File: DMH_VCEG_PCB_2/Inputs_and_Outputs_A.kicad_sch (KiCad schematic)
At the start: 39 parts, among them J1 TS_Jack_6.35mm_Sw, J10 TS_Jack_6.35mm_Sw, J2 TS_Jack_6.35mm_Sw, J200 IDC_02x08, J21 Conn_01x10_PinHeader, J22 Conn_01x10_PinHeader, J23 Conn_01x10_PinHeader, J27 Conn_01x06_PinHeader, J3 TS_Jack_6.35mm_Sw, J4 TS_Jack_6.35mm_Sw, J5 TS_Jack_6.35mm_Sw, J6 TS_Jack_6.35mm_Sw, J7 TS_Jack_6.35mm_Sw, J8 TS_Jack_6.35mm_Sw, J9 TS_Jack_6.35mm_Sw, U21 TL074, U9 TL074

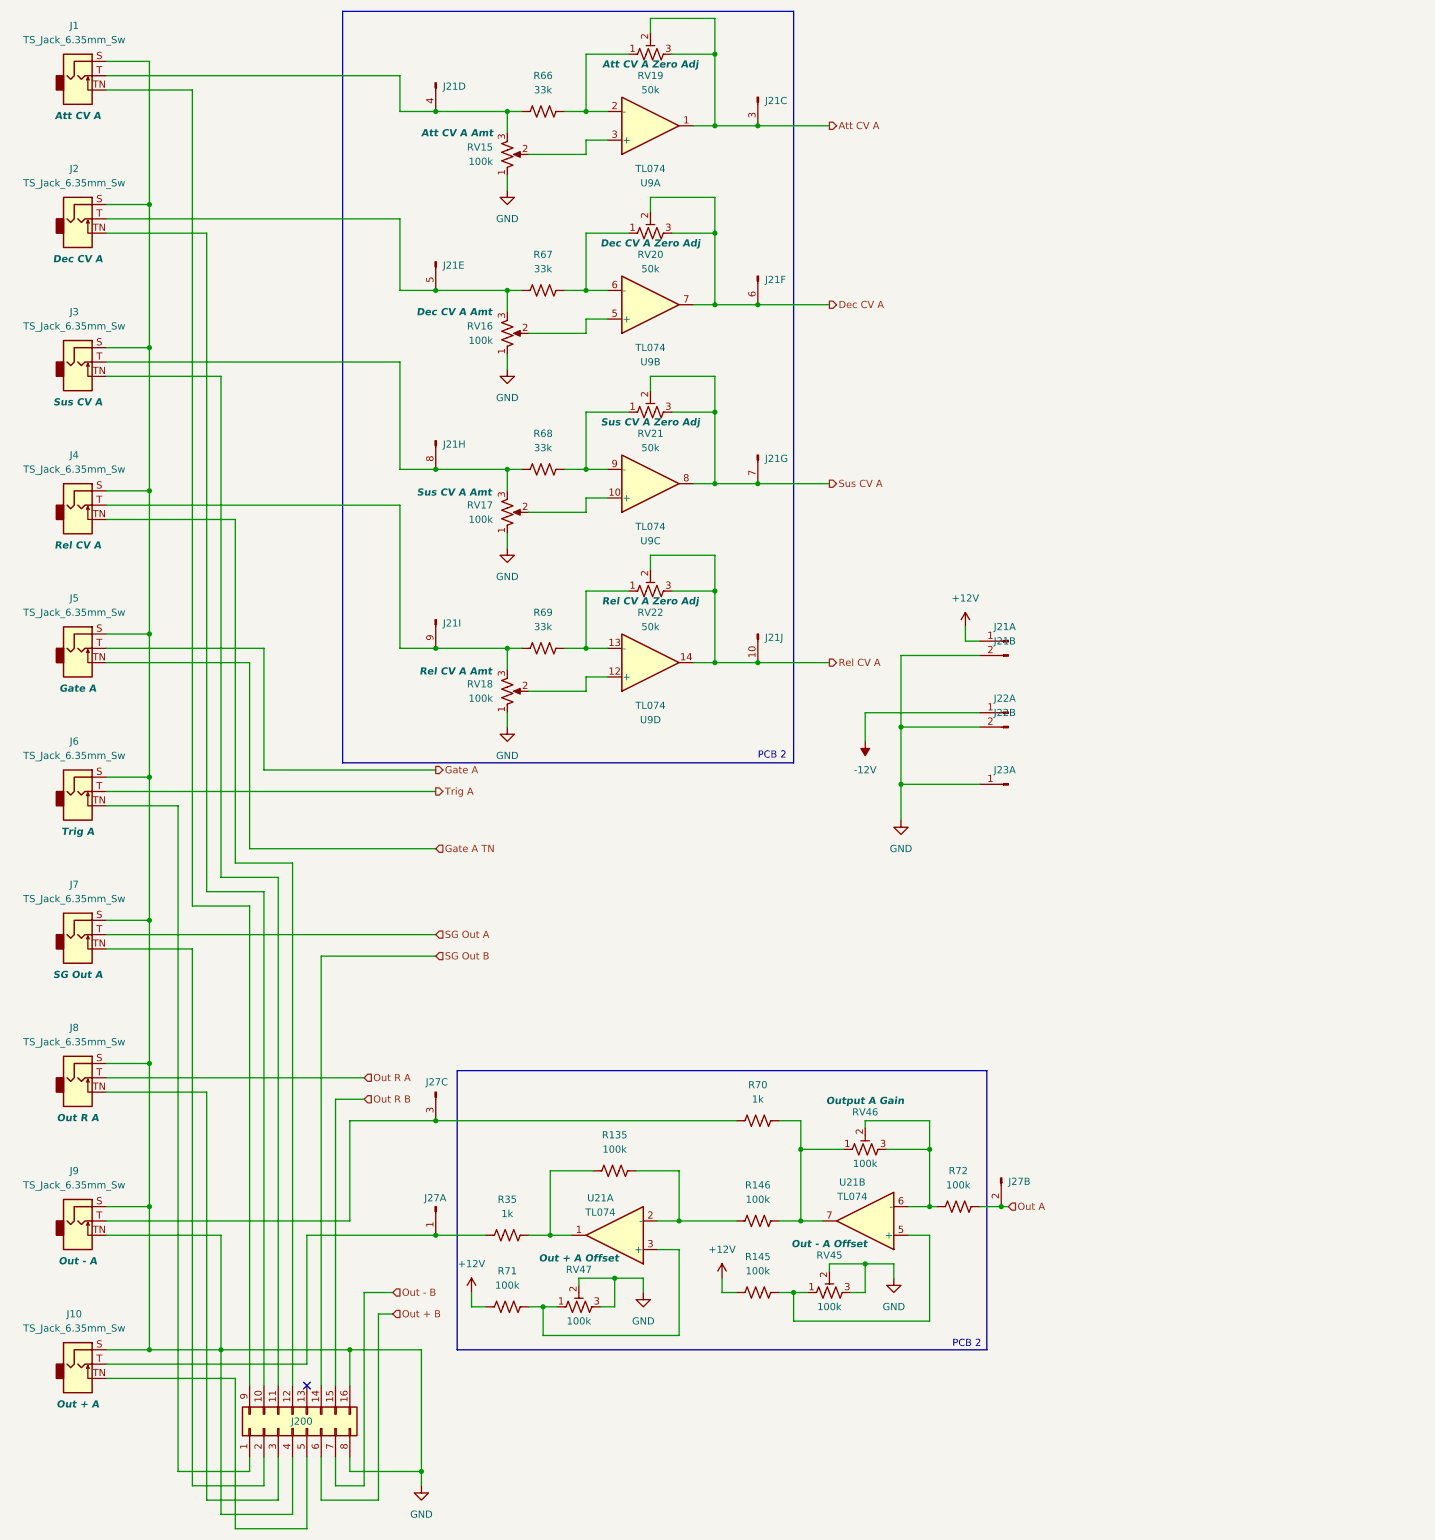
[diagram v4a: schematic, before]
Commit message: Fixed mistake in IO connections
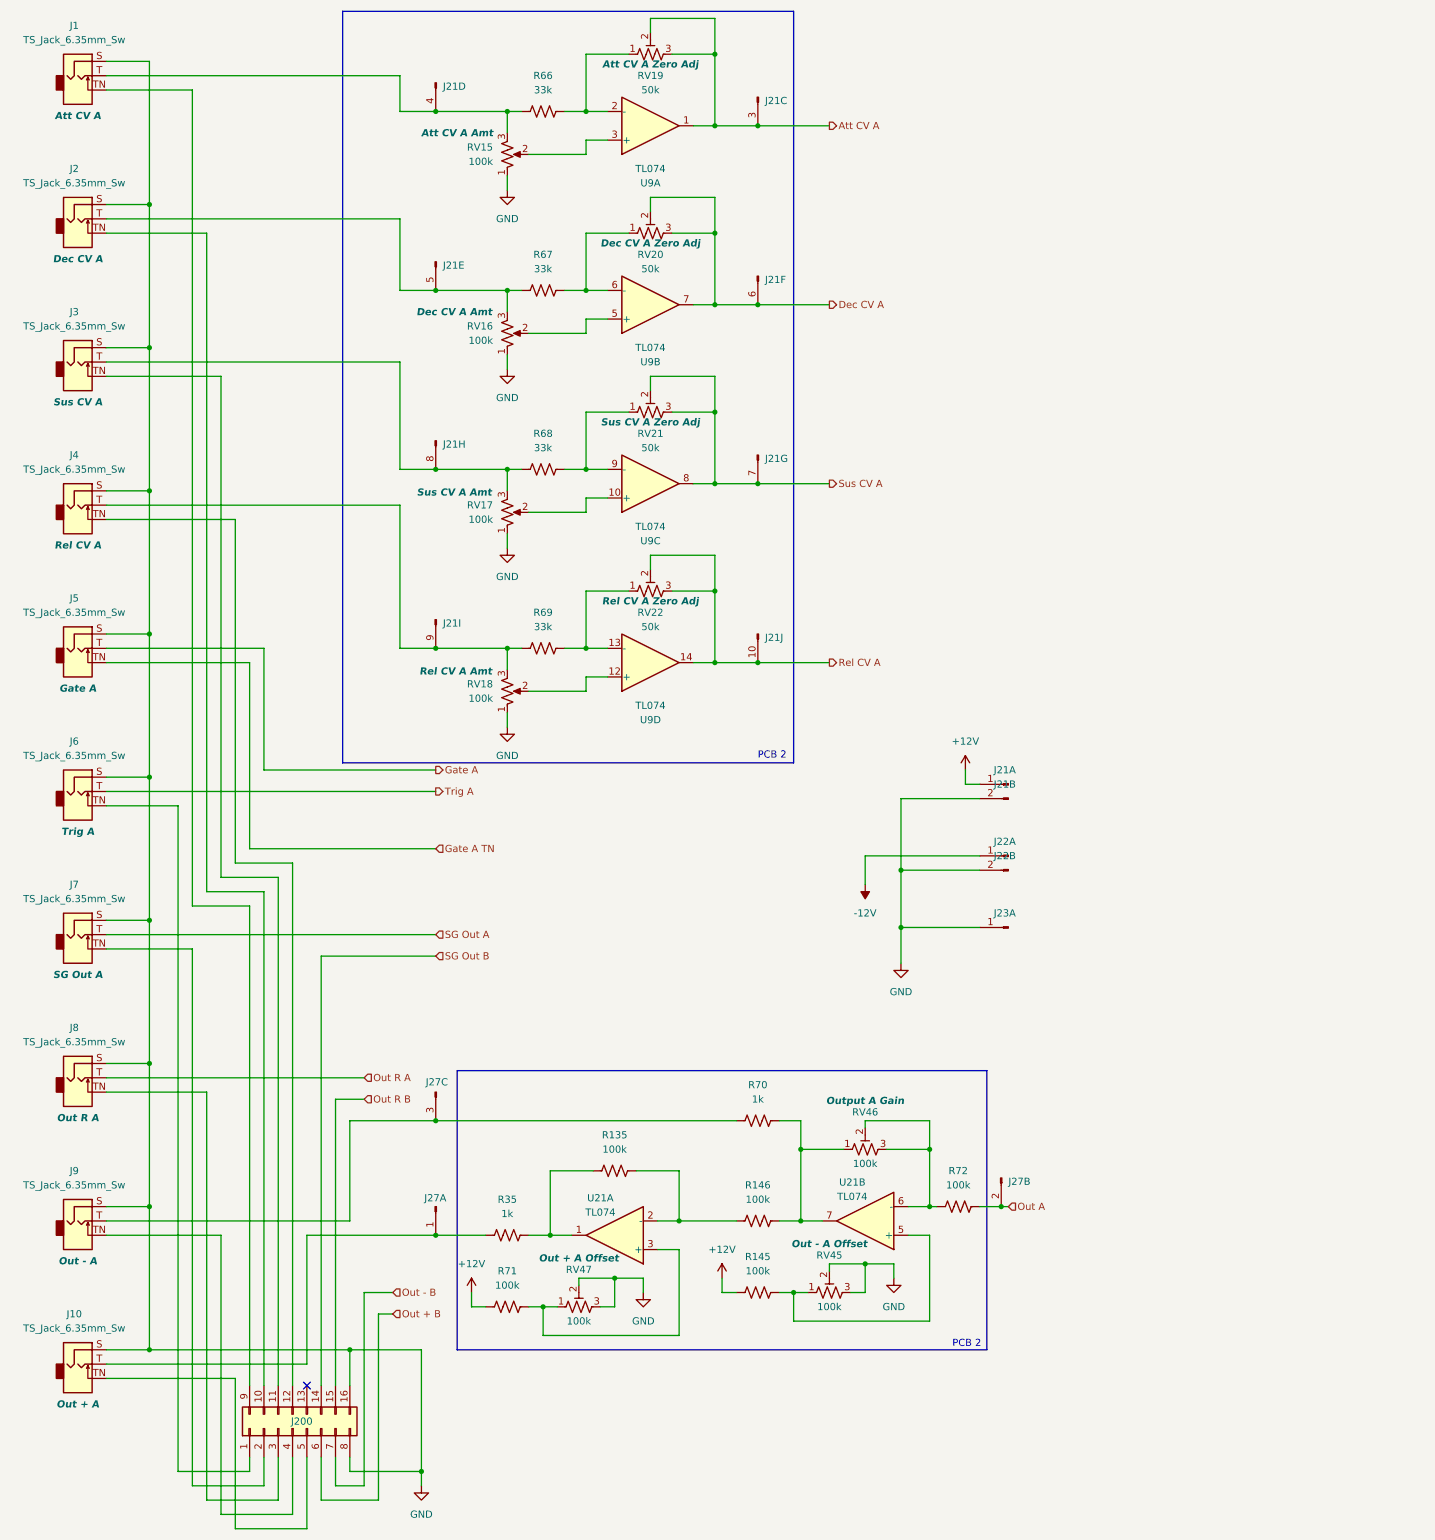
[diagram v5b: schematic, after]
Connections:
- net GND: no longer J200.4 (Pin_4), J9.TN
- new net: J200.4 (Pin_4), J9.TN
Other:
- moved on the sheet: J21A, J21B, J22A, J22B, J23A
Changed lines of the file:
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@@
 	)
 	(junction
-		(at 171.45 151.13)
+		(at 171.45 176.53)
 		(diameter 0)
 		(color 0 0 0 0)
@@
 	)
 	(junction
-		(at 171.45 140.97)
+		(at 171.45 166.37)
 		(diameter 0)
 		(color 0 0 0 0)
@@
 	)
 	(junction
-		(at 50.8 251.46)
-		(diameter 0)
-		(color 0 0 0 0)
-	)
-	(junction
 		(at 146.05 66.04)
 		(diameter 0)
@@
 	(wire
 		(pts
-			(xy 185.42 140.97) (xy 171.45 140.97)
+			(xy 185.42 166.37) (xy 171.45 166.37)
 		)
 		(stroke
@@
 	(wire
 		(pts
-			(xy 50.8 231.14) (xy 50.8 251.46)
+			(xy 50.8 231.14) (xy 50.8 280.67)
 		)
 		(stroke
@@
 	(wire
 		(pts
-			(xy 185.42 138.43) (xy 165.1 138.43)
+			(xy 185.42 163.83) (xy 165.1 163.83)
 		)
 		(stroke
@@
 	(wire
 		(pts
-			(xy 171.45 151.13) (xy 185.42 151.13)
+			(xy 171.45 176.53) (xy 185.42 176.53)
 		)
 		(stroke
@@
 	(wire
 		(pts
-			(xy 50.8 251.46) (xy 50.8 280.67)
-		)
-		(stroke
-			(width 0)
-			(type default)
-		)
-	)
-	(wire
-		(pts
 			(xy 139.7 241.3) (xy 142.24 241.3)
 		)
@@
 	(wire
 		(pts
-			(xy 185.42 128.27) (xy 171.45 128.27)
+			(xy 185.42 153.67) (xy 171.45 153.67)
 		)
 		(stroke
@@
 	(wire
 		(pts
-			(xy 171.45 140.97) (xy 171.45 151.13)
+			(xy 171.45 166.37) (xy 171.45 176.53)
 		)
 		(stroke
@@
 	(wire
 		(pts
-			(xy 171.45 128.27) (xy 171.45 140.97)
+			(xy 171.45 153.67) (xy 171.45 166.37)
 		)
 		(stroke
@@
 	(wire
 		(pts
-			(xy 50.8 251.46) (xy 38.1 251.46)
+			(xy 38.1 251.46) (xy 73.66 251.46)
 		)
 		(stroke
@@
 	(wire
 		(pts
-			(xy 182.88 123.19) (xy 182.88 125.73)
+			(xy 182.88 148.59) (xy 182.88 151.13)
 		)
 		(stroke
@@
 	(wire
 		(pts
-			(xy 165.1 138.43) (xy 165.1 143.51)
+			(xy 165.1 163.83) (xy 165.1 168.91)
 		)
 		(stroke
@@
 	(wire
 		(pts
-			(xy 185.42 125.73) (xy 182.88 125.73)
+			(xy 185.42 151.13) (xy 182.88 151.13)
 		)
 		(stroke
@@
 	(wire
 		(pts
-			(xy 171.45 151.13) (xy 171.45 157.48)
+			(xy 171.45 176.53) (xy 171.45 182.88)
 		)
 		(stroke
@@
 	(wire
 		(pts
-			(xy 50.8 251.46) (xy 73.66 251.46)
-		)
-		(stroke
-			(width 0)
-			(type default)
-		)
-	)
-	(wire
-		(pts
 			(xy 82.55 25.4) (xy 82.55 31.75)
 		)
@@
 	(symbol
 		(lib_id "SynthStuff:Conn_01x10_PinHeader")
-		(at 190.5 138.43 180)
+		(at 190.5 163.83 180)
 		(unit 1)
 		(exclude_from_sim no)
@@
 		(fields_autoplaced yes)
 		(property "Reference" "J22"
-			(at 189.865 135.89 0)
+			(at 189.865 161.29 0)
 			(effects
 				(font
@@
 		)
 		(property "Value" "Conn_01x10_PinHeader"
-			(at 190.5 135.89 0)
+			(at 190.5 161.29 0)
 			(effects
 				(font
@@
 		)
 		(property "Footprint" "Connector_PinSocket_2.54mm:PinSocket_1x10_P2.54mm_Vertical"
-			(at 190.5 138.43 0)
+			(at 190.5 163.83 0)
 			(effects
 				(font
@@
 		)
 		(property "Datasheet" "~"
-			(at 190.5 138.43 0)
+			(at 190.5 163.83 0)
 			(effects
 				(font
@@
 		)
 		(property "Description" "Generic connector, single row, 01x10"
-			(at 190.5 138.43 0)
+			(at 190.5 163.83 0)
 			(effects
 				(font
@@
 	(symbol
 		(lib_id "SynthStuff:Conn_01x10_PinHeader")
-		(at 190.5 125.73 180)
+		(at 190.5 151.13 180)
 		(unit 1)
 		(exclude_from_sim no)
@@
 		(fields_autoplaced yes)
 		(property "Reference" "J21"
-			(at 189.865 123.19 0)
+			(at 189.865 148.59 0)
 			(effects
 				(font
@@
 		)
 		(property "Value" "Conn_01x10_PinHeader"
-			(at 190.5 123.19 0)
+			(at 190.5 148.59 0)
 			(effects
 				(font
@@
 		)
 		(property "Footprint" "Connector_PinSocket_2.54mm:PinSocket_1x10_P2.54mm_Vertical"
-			(at 190.5 125.73 0)
+			(at 190.5 151.13 0)
 			(effects
 				(font
@@
 		)
 		(property "Datasheet" "~"
-			(at 190.5 125.73 0)
+			(at 190.5 151.13 0)
 			(effects
 				(font
@@
 		)
 		(property "Description" "Generic connector, single row, 01x10"
-			(at 190.5 125.73 0)
+			(at 190.5 151.13 0)
 			(effects
 				(font
@@
 	(symbol
 		(lib_id "SynthStuff:Conn_01x10_PinHeader")
-		(at 190.5 151.13 180)
+		(at 190.5 176.53 180)
 		(unit 1)
 		(exclude_from_sim no)
@@
 		(fields_autoplaced yes)
 		(property "Reference" "J23"
-			(at 189.865 148.59 0)
+			(at 189.865 173.99 0)
 			(effects
 				(font
@@
 		)
 		(property "Value" "Conn_01x10_PinHeader"
-			(at 190.5 148.59 0)
+			(at 190.5 173.99 0)
 			(effects
 				(font
@@
 		)
 		(property "Footprint" "Connector_PinSocket_2.54mm:PinSocket_1x10_P2.54mm_Vertical"
-			(at 190.5 151.13 0)
+			(at 190.5 176.53 0)
 			(effects
 				(font
@@
 		)
 		(property "Datasheet" "~"
-			(at 190.5 151.13 0)
+			(at 190.5 176.53 0)
 			(effects
 				(font
@@
 		)
 		(property "Description" "Generic connector, single row, 01x10"
-			(at 190.5 151.13 0)
+			(at 190.5 176.53 0)
 			(effects
 				(font
@@
 	(symbol
 		(lib_id "power:GND")
-		(at 171.45 157.48 0)
+		(at 171.45 182.88 0)
 		(unit 1)
 		(exclude_from_sim no)
@@
 		(fields_autoplaced yes)
 		(property "Reference" "#PWR096"
-			(at 171.45 163.83 0)
+			(at 171.45 189.23 0)
 			(effects
 				(font
@@
 		)
 		(property "Value" "GND"
-			(at 171.45 162.56 0)
+			(at 171.45 187.96 0)
 			(effects
 				(font
@@
 		)
 		(property "Footprint" ""
-			(at 171.45 157.48 0)
+			(at 171.45 182.88 0)
 			(effects
 				(font
@@
 		)
 		(property "Datasheet" ""
-			(at 171.45 157.48 0)
+			(at 171.45 182.88 0)
 			(effects
 				(font
@@
 		)
 		(property "Description" "Power symbol creates a global label with name \"GND\" , ground"
-			(at 171.45 157.48 0)
+			(at 171.45 182.88 0)
 			(effects
 				(font
@@
 	(symbol
 		(lib_id "power:-12V")
-		(at 165.1 143.51 180)
+		(at 165.1 168.91 180)
 		(unit 1)
 		(exclude_from_sim no)
@@
 		(fields_autoplaced yes)
 		(property "Reference" "#PWR098"
-			(at 165.1 139.7 0)
+			(at 165.1 165.1 0)
 			(effects
 				(font
@@
 		)
 		(property "Value" "-12V"
-			(at 165.1 148.59 0)
+			(at 165.1 173.99 0)
 			(effects
 				(font
@@
 		)
 		(property "Footprint" ""
-			(at 165.1 143.51 0)
+			(at 165.1 168.91 0)
 			(effects
 				(font
@@
 		)
 		(property "Datasheet" ""
-			(at 165.1 143.51 0)
+			(at 165.1 168.91 0)
 			(effects
 				(font
@@
 		)
 		(property "Description" "Power symbol creates a global label with name \"-12V\""
-			(at 165.1 143.51 0)
+			(at 165.1 168.91 0)
 			(effects
 				(font
@@
 	(symbol
 		(lib_id "SynthStuff:Conn_01x10_PinHeader")
-		(at 190.5 128.27 180)
+		(at 190.5 153.67 180)
 		(unit 2)
 		(exclude_from_sim no)
@@
 		(fields_autoplaced yes)
 		(property "Reference" "J21"
-			(at 189.865 125.73 0)
+			(at 189.865 151.13 0)
 			(effects
 				(font
@@
 		)
 		(property "Value" "Conn_01x10_PinHeader"
-			(at 190.5 125.73 0)
+			(at 190.5 151.13 0)
 			(effects
 				(font
@@
 		)
 		(property "Footprint" "Connector_PinSocket_2.54mm:PinSocket_1x10_P2.54mm_Vertical"
-			(at 190.5 128.27 0)
+			(at 190.5 153.67 0)
 			(effects
 				(font
@@
 		)
 		(property "Datasheet" "~"
-			(at 190.5 128.27 0)
+			(at 190.5 153.67 0)
 			(effects
 				(font
@@
 		)
 		(property "Description" "Generic connector, single row, 01x10"
-			(at 190.5 128.27 0)
+			(at 190.5 153.67 0)
 			(effects
 				(font
@@
 	(symbol
 		(lib_id "power:+12V")
-		(at 182.88 123.19 0)
+		(at 182.88 148.59 0)
 		(unit 1)
 		(exclude_from_sim no)
@@
 		(fields_autoplaced yes)
 		(property "Reference" "#PWR095"
-			(at 182.88 127 0)
+			(at 182.88 152.4 0)
 			(effects
 				(font
@@
 		)
 		(property "Value" "+12V"
-			(at 182.88 118.11 0)
+			(at 182.88 143.51 0)
 			(effects
 				(font
@@
 		)
 		(property "Footprint" ""
-			(at 182.88 123.19 0)
+			(at 182.88 148.59 0)
 			(effects
 				(font
@@
 		)
 		(property "Datasheet" ""
-			(at 182.88 123.19 0)
+			(at 182.88 148.59 0)
 			(effects
 				(font
@@
 		)
 		(property "Description" "Power symbol creates a global label with name \"+12V\""
-			(at 182.88 123.19 0)
+			(at 182.88 148.59 0)
 			(effects
 				(font
@@
 	(symbol
 		(lib_id "SynthStuff:Conn_01x10_PinHeader")
-		(at 190.5 140.97 180)
+		(at 190.5 166.37 180)
 		(unit 2)
 		(exclude_from_sim no)
@@
 		(fields_autoplaced yes)
 		(property "Reference" "J22"
-			(at 189.865 138.43 0)
+			(at 189.865 163.83 0)
 			(effects
 				(font
@@
 		)
 		(property "Value" "Conn_01x10_PinHeader"
-			(at 190.5 138.43 0)
+			(at 190.5 163.83 0)
 			(effects
 				(font
@@
 		)
 		(property "Footprint" "Connector_PinSocket_2.54mm:PinSocket_1x10_P2.54mm_Vertical"
-			(at 190.5 140.97 0)
+			(at 190.5 166.37 0)
 			(effects
 				(font
@@
 		)
 		(property "Datasheet" "~"
-			(at 190.5 140.97 0)
+			(at 190.5 166.37 0)
 			(effects
 				(font
@@
 		)
 		(property "Description" "Generic connector, single row, 01x10"
-			(at 190.5 140.97 0)
+			(at 190.5 166.37 0)
 			(effects
 				(font
